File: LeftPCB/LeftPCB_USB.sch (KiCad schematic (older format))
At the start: 62 parts, among them IC1 FE1.1S, SW1 LID_SW, SW2 USB_BSL, SW3 RESET, U1 4011, U2 MSP430F5508IRGZ, Y1 12Mhz, Y2 12Mhz

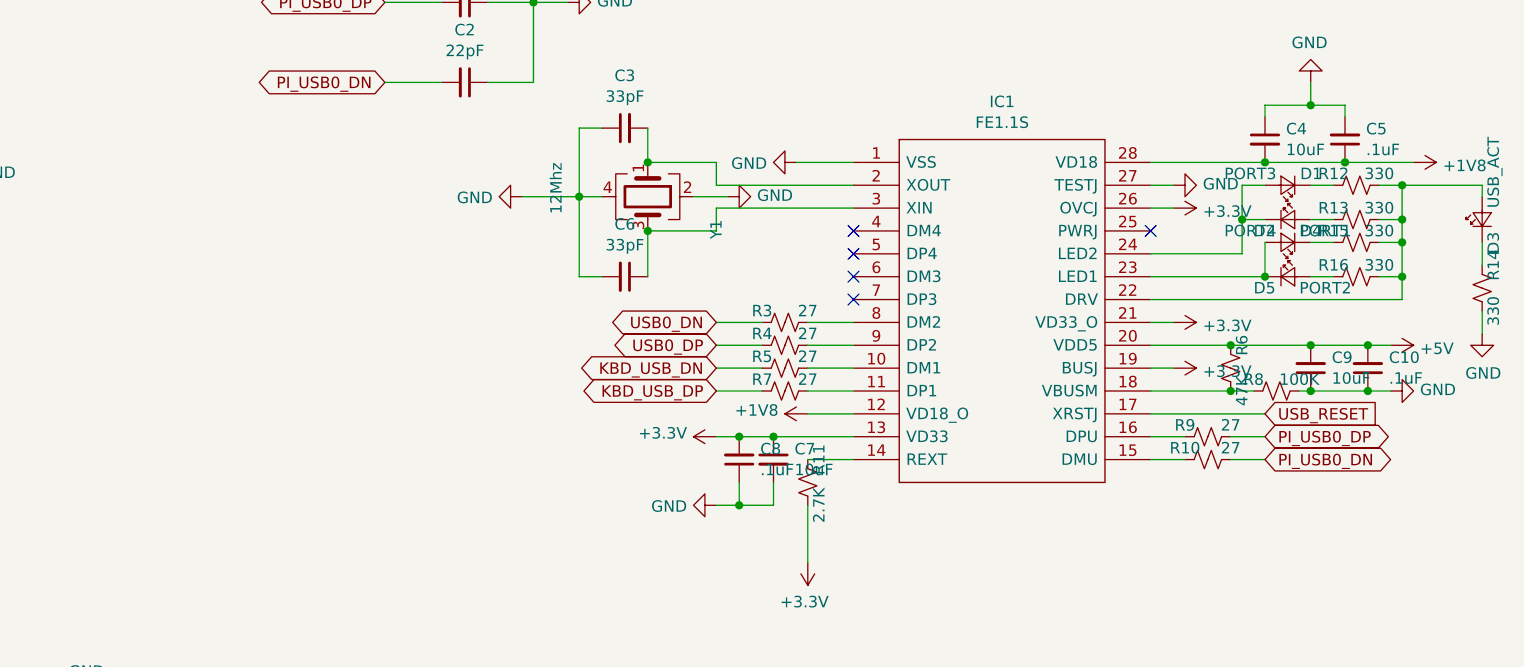
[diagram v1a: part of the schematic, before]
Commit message: Completed most of left side schematic and started working on layout.
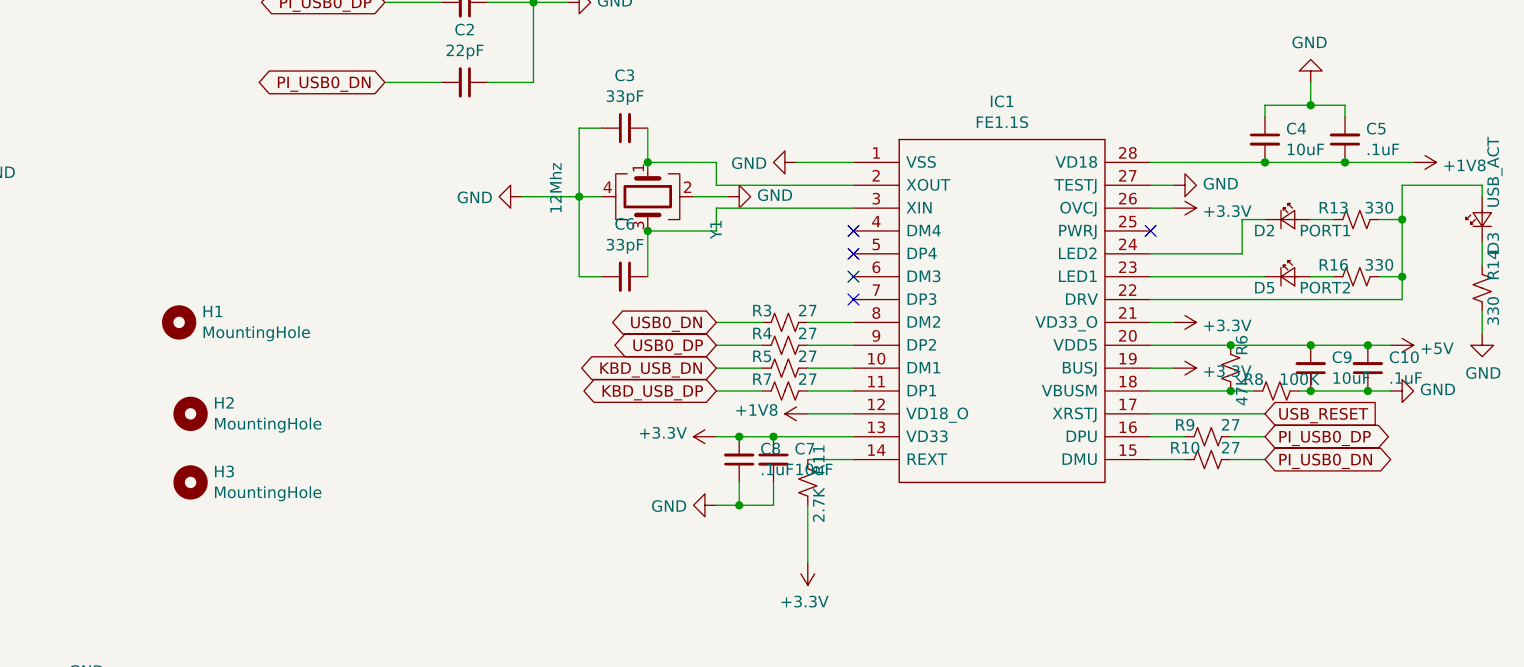
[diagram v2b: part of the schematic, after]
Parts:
- removed D1: PORT3, LEDs:LED_0805, symbol Device:LED_Small
- removed D4: PORT4, LEDs:LED_0805, symbol Device:LED_Small
- removed R12, R15: 330, Resistors_SMD:R_0603, symbol Device:R_Small_US
- added H1, H2, H3: MountingHole, Mounting_Holes:MountingHole_2.7mm, symbol Mechanical:MountingHole
- U2: footprint Housings_DFN_QFN:QFN-28-1EP_5x5mm_Pitch0.5mm -> MSP430F5508IRGCR:QFN50P900X900X100-65N
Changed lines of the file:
@@
 F 0 "U2" H 4900 4500 50  0000 C CNN
 F 1 "MSP430F5508IRGZ" H 5200 4600 50  0000 C CNN
-F 2 "Housings_DFN_QFN:QFN-28-1EP_5x5mm_Pitch0.5mm" H 3500 4650 50  0001 C CIN
+F 2 "MSP430F5508IRGCR:QFN50P900X900X100-65N" H 3500 4650 50  0001 C CIN
 F 3 "http://www.ti.com/lit/ds/symlink/msp430f5508.pdf" H 4400 5800 50  0001 C CNN
 	1    4350 5800
@@
 	9650 1600 9750 1600
 $Comp
-L Device:LED_Small D1
-U 1 1 5EB27187
-P 10250 1600
-F 0 "D1" H 10100 1550 50  0000 L CNN
-F 1 "PORT3" H 10300 1550 50  0000 L CNN
-F 2 "LEDs:LED_0805" V 10250 1600 50  0001 C CNN
-F 3 "~" V 10250 1600 50  0001 C CNN
-	1    10250 1600
-	-1   0    0    1
-$EndComp
-$Comp
 L Device:LED_Small D2
 U 1 1 5EB28765
@@
 	1    10250 1750
 	1    0    0    -1
-$EndComp
-$Comp
-L Device:LED_Small D4
-U 1 1 5EB28C27
-P 10250 1850
-F 0 "D4" H 10100 1800 50  0000 L CNN
-F 1 "PORT4" H 10300 1800 50  0000 L CNN
-F 2 "LEDs:LED_0805" V 10250 1850 50  0001 C CNN
-F 3 "~" V 10250 1850 50  0001 C CNN
-	1    10250 1850
-	-1   0    0    1
 $EndComp
 $Comp
@@
 $EndComp
 $Comp
-L Device:R_Small_US R12
-U 1 1 5EB29CA9
-P 10550 1600
-F 0 "R12" V 10500 1500 50  0000 C CNN
-F 1 "330" V 10500 1700 50  0000 C CNN
-F 2 "Resistors_SMD:R_0603" H 10550 1600 50  0001 C CNN
-F 3 "~" H 10550 1600 50  0001 C CNN
-	1    10550 1600
-	0    1    1    0
-$EndComp
-$Comp
 L Device:R_Small_US R13
 U 1 1 5EB2A0BD
@@
 F 3 "~" H 10550 1750 50  0001 C CNN
 	1    10550 1750
-	0    1    1    0
-$EndComp
-$Comp
-L Device:R_Small_US R15
-U 1 1 5EB2A2F4
-P 10550 1850
-F 0 "R15" V 10500 1750 50  0000 C CNN
-F 1 "330" V 10500 1950 50  0000 C CNN
-F 2 "Resistors_SMD:R_0603" H 10550 1850 50  0001 C CNN
-F 3 "~" H 10550 1850 50  0001 C CNN
-	1    10550 1850
 	0    1    1    0
 $EndComp
@@
 	10050 1900 10050 1750
 Wire Wire Line
-	10050 1600 10150 1600
-Wire Wire Line
 	9650 1900 10050 1900
 Wire Wire Line
 	10150 1750 10050 1750
-Connection ~ 10050 1750
-Wire Wire Line
-	10050 1750 10050 1600
-Wire Wire Line
-	10350 1600 10450 1600
 Wire Wire Line
 	10450 1750 10350 1750
 Wire Wire Line
 	9650 2000 10150 2000
-Connection ~ 10150 2000
-Wire Wire Line
-	10150 1850 10150 2000
-Wire Wire Line
-	10350 1850 10450 1850
 Wire Wire Line
 	10450 2000 10350 2000
 Wire Wire Line
 	10750 2100 10750 2000
-Wire Wire Line
-	10750 1600 10650 1600
 Wire Wire Line
 	9650 2100 10750 2100
@@
 	10750 1750 10750 1600
 Wire Wire Line
-	10650 1850 10750 1850
-Connection ~ 10750 1850
-Wire Wire Line
-	10750 1850 10750 1750
-Wire Wire Line
 	10650 2000 10750 2000
 Connection ~ 10750 2000
 Wire Wire Line
-	10750 2000 10750 1850
-Wire Wire Line
 	11100 1650 11100 1600
 Wire Wire Line
 	11100 1600 10750 1600
-Connection ~ 10750 1600
 Wire Wire Line
 	11100 1850 11100 1950
@@
 Wire Wire Line
 	3200 6100 3000 6100
+$Comp
+L Mechanical:MountingHole H1
+U 1 1 5EFBD3B6
+P 5400 2200
+F 0 "H1" H 5500 2246 50  0000 L CNN
+F 1 "MountingHole" H 5500 2155 50  0000 L CNN
+F 2 "Mounting_Holes:MountingHole_2.7mm" H 5400 2200 50  0001 C CNN
+F 3 "~" H 5400 2200 50  0001 C CNN
+	1    5400 2200
+	1    0    0    -1
+$EndComp
+$Comp
+L Mechanical:MountingHole H2
+U 1 1 5EFBD795
+P 5450 2600
+F 0 "H2" H 5550 2646 50  0000 L CNN
+F 1 "MountingHole" H 5550 2555 50  0000 L CNN
+F 2 "Mounting_Holes:MountingHole_2.7mm" H 5450 2600 50  0001 C CNN
+F 3 "~" H 5450 2600 50  0001 C CNN
+	1    5450 2600
+	1    0    0    -1
+$EndComp
+$Comp
+L Mechanical:MountingHole H3
+U 1 1 5EFF6A88
+P 5450 2900
+F 0 "H3" H 5550 2946 50  0000 L CNN
+F 1 "MountingHole" H 5550 2855 50  0000 L CNN
+F 2 "Mounting_Holes:MountingHole_2.7mm" H 5450 2900 50  0001 C CNN
+F 3 "~" H 5450 2900 50  0001 C CNN
+	1    5450 2900
+	1    0    0    -1
+$EndComp
+Wire Wire Line
+	10750 1750 10750 2000
 $EndSCHEMATC

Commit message: Updated and performed layout on most of left PCB, still have a few things to add.
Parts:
- removed R27: 1M, Resistors_SMD:R_0603, symbol Device:R_Small_US
- added J5: PI_USB0, Pin_Headers:Pin_Header_Straight_1x04_Pitch1.00mm, symbol Connector_Generic:Conn_01x04
- U2: footprint MSP430F5508IRGCR:QFN50P900X900X100-65N -> Housings_QFP:LQFP-48_7x7mm_Pitch0.5mm
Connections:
- net BRIGHTNESS: now also U2.3 (P6.2/CB2/A2); no longer U2.1 (P6.0/CB0/A0)
- net GND: now also R18.1, R19.1, R20.1, J5.1 (Pin_1); no longer R18.2, R19.2, R20.2
- net IS_PWR_DWN: now also U2.16 (TA0.1/P1.2); no longer U2.21 (TA1.0/P1.7)
- net KBD_COL_SEL_0: now also U2.24 (PJ.1/TDI/TCLK); no longer U2.14 (TA0CLK/ACLK/P1.0)
- net KBD_COL_SEL_1: now also U2.22 (TA1.1/P2.0); no longer U2.15 (TA0.0/P1.1)
- net KBD_COL_SEL_2: now also U2.30 (PM_UCB1SIMO/PM_UCB1SDA/P4.1); no longer U2.16 (TA0.1/P1.2)
- net KBD_COL_SEL_3: now also U2.26 (PJ.3/TCK); no longer U2.17 (TA0.2/P1.3)
- net KBD_COL_VAL: now also U2.32 (PM_UCB1CLK/PM_UCA1STE/P4.3); no longer U2.18 (TA0.3/P1.4)
- net KBD_ROW_0: now also U2.19 (TA0.4/P1.5); no longer U2.29 (PM_UCB1STE/PM_UCA1CLK/P4.0)
- net KBD_ROW_1: now also U2.20 (TA1CLK/CBOUT/P1.6); no longer U2.30 (PM_UCB1SIMO/PM_UCB1SDA/P4.1)
- net KBD_ROW_2: now also U2.21 (TA1.0/P1.7); no longer U2.31 (PM_UCB1SOMI/PM_UCB1SCL/P4.2)
- net KBD_ROW_3: now also U2.23 (PJ.0/TDO); no longer U2.32 (PM_UCB1CLK/PM_UCA1STE/P4.3)
- net KBD_ROW_4: now also U2.25 (PJ.2/TMS); no longer U2.33 (PM_UCA1TXD/PM_UCA1SIMO/P4.4)
- net KBD_ROW_5: now also U2.29 (PM_UCB1STE/PM_UCA1CLK/P4.0); no longer U2.34 (PM_UCA1RXD/PM_UCA1SOMI/P4.5)
- net KBD_ROW_6: now also U2.31 (PM_UCB1SOMI/PM_UCB1SCL/P4.2); no longer U2.35 (P4.6)
- net KBD_ROW_7: now also U2.33 (PM_UCA1TXD/PM_UCA1SIMO/P4.4); no longer U2.36 (P4.7)
- net PI_SHUTDOWN: now also U2.17 (TA0.2/P1.3); no longer U2.20 (TA1CLK/CBOUT/P1.6)
- net PI_USB0_DN: now also J5.2 (Pin_2)
- net PI_USB0_DP: now also J5.3 (Pin_3)
- net SYS_PWR_EN: now also U2.18 (TA0.3/P1.4); no longer U2.22 (TA1.1/P2.0)
- net USB_RESET: now also U2.14 (TA0CLK/ACLK/P1.0); no longer U2.19 (TA0.4/P1.5)
- net at D8.2 (A): now also U2.36 (P4.7); no longer U2.24 (PJ.1/TDI/TCLK)
- net at D7.2 (A): now also U2.35 (P4.6); no longer U2.25 (PJ.2/TMS)
- net at D6.2 (A): now also U2.34 (PM_UCA1RXD/PM_UCA1SOMI/P4.5); no longer U2.26 (PJ.3/TCK)
- net at D6.1 (K): now also R18.2; no longer R18.1
- net at D7.1 (K): now also R19.2; no longer R19.1
- net at D8.1 (K): now also R20.2; no longer R20.1
- no-connect marks 10 -> 12
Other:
- moved on the sheet: D6, D7, D8, R18, R19, R20, R26
